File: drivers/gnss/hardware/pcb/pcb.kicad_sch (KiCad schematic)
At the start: 41 parts, among them J1 POWER, J2 SMA, J3 SMA, J4 RS485, U1 AMS1117-3.3, U2 LC02H, U3 74HC14, U4 MAX3485

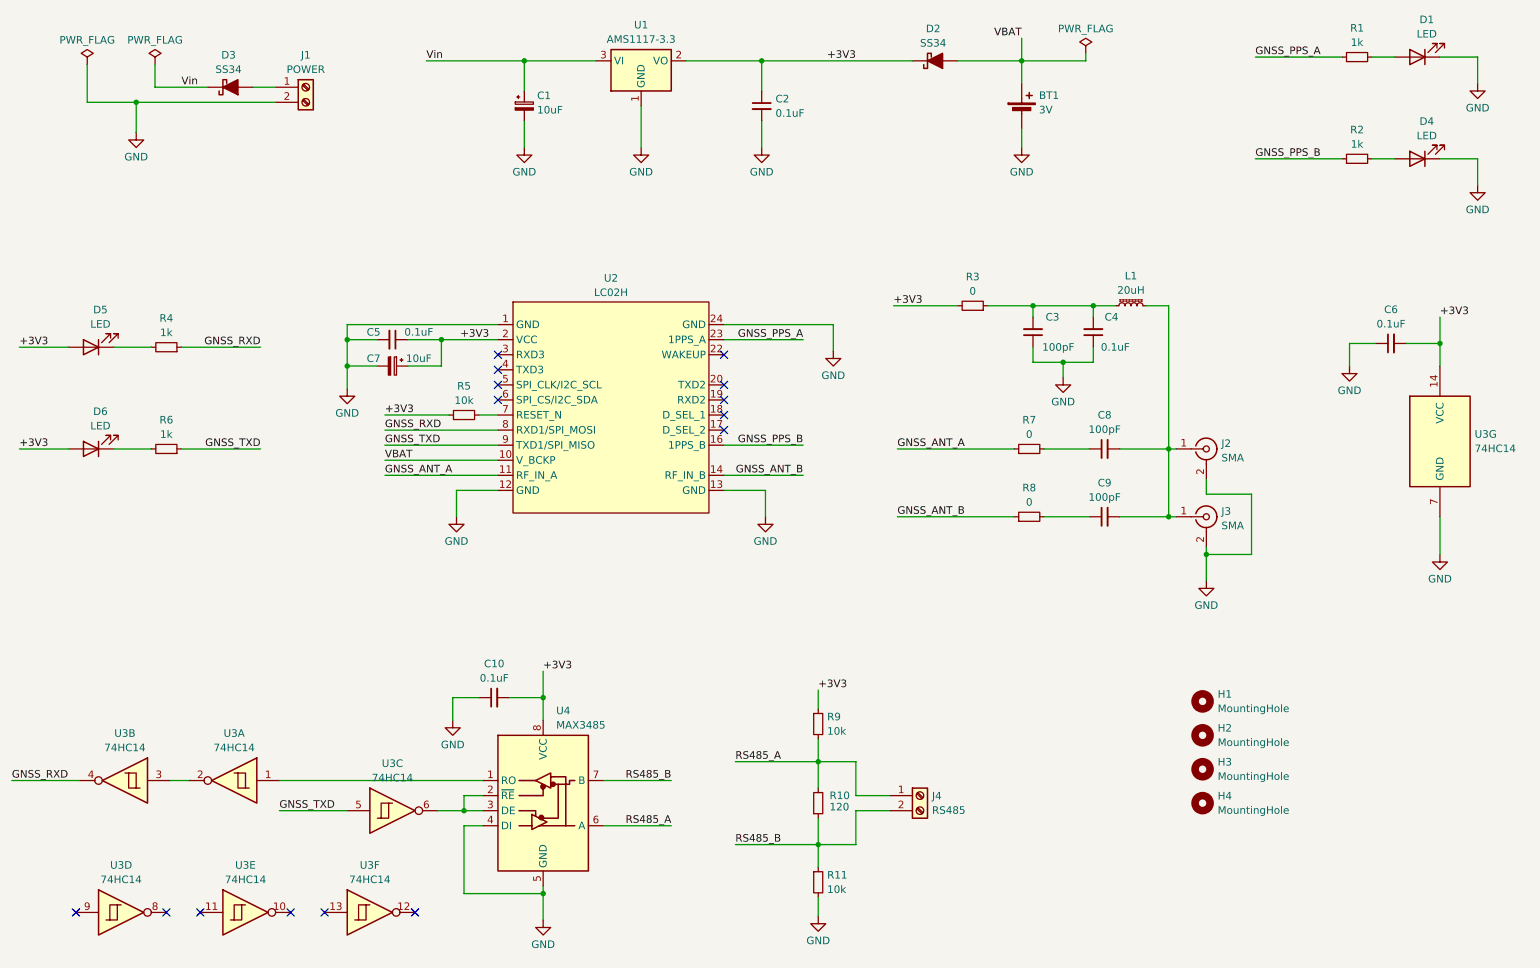
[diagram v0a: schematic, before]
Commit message: Add LNA schematic & PCB design
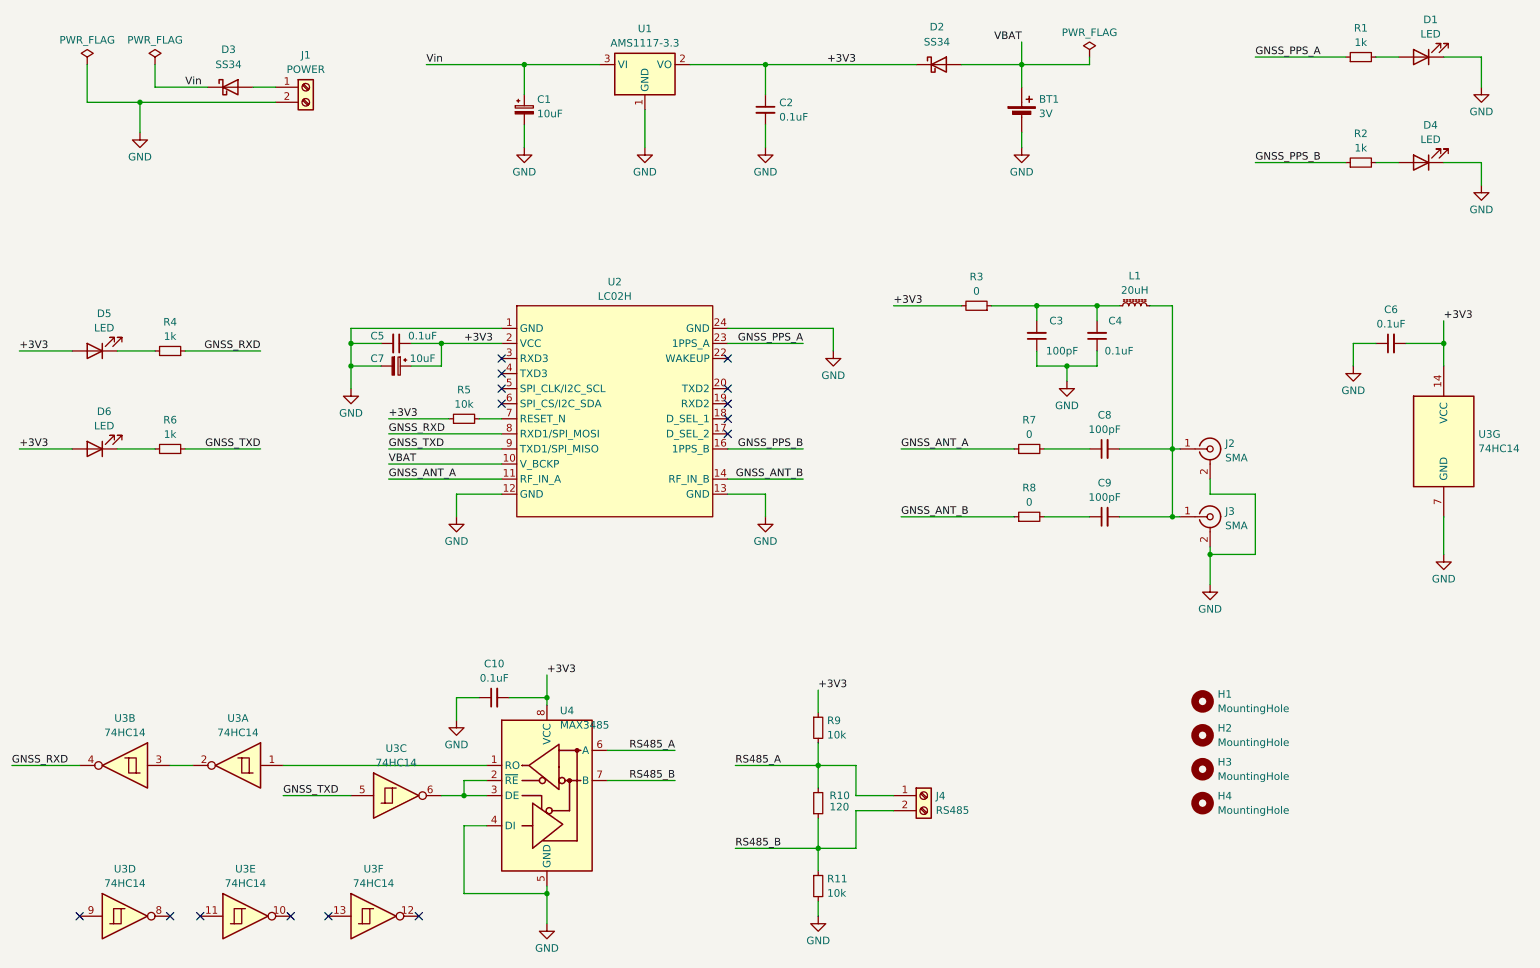
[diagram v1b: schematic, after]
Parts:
- removed D2, D3: SS34, Diode_SMD:D_SMA, symbol PCM_Diode_Schottky_AKL:SS34
- added D2, D3: SS34, Diode_SMD:D_SMA, symbol Diode:SS34
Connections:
- net +3V3: now also D2.1 (K)
- net VBAT: now also D2.2 (A)
- net Vin: now also D3.1 (K)
- net at J1.1 (Pin_1): now also D3.2 (A)
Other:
- moved on the sheet: BT1, C1, C2, C3, C4, C5, C7, D1, D4, D5, D6, J2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

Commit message: Update GNSS PCB
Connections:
- net +3V3: now also D2.2 (A); no longer D2.1 (K)
- net VBAT: now also D2.1 (K); no longer D2.2 (A)
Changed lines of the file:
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@@
 		(lib_id "Diode:SS34")
 		(at 173.99 33.02 0)
+		(mirror y)
 		(unit 1)
 		(exclude_from_sim no)
@@
 		(on_board yes)
 		(dnp no)
-		(fields_autoplaced yes)
 		(property "Reference" "D2"
-			(at 173.6725 26.67 0)
+			(at 174.3075 26.67 0)
 			(effects
 				(font
@@
 		)
 		(property "Value" "SS34"
-			(at 173.6725 29.21 0)
+			(at 174.3075 29.21 0)
 			(effects
 				(font
